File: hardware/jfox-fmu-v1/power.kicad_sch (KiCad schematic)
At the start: 7 parts, among them U20 LTC4417CGN, U21 TPS62132, U22 AP2112K-3.3, U23 AP22804AW5, U24 AP22804AW5, U25 AP22804AW5, U26 AP22804AW5

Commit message: Isolated CAN FD, and the short it took a bisect to find
CAN redundancy is resolved by using Cyphal. FDCAN1 and FDCAN2 become two
redundant Cyphal/CAN interfaces on two independent isolated buses.

That is not the compromise it looked like. Cyphal handles redundancy in the
protocol: the specification defines redundant transport groups where a node
publishes on every interface and the receiver deduplicates, per frame or per
transfer. libcanard gives each redundant interface its own TX queue for
exactly this. So two controllers is the arrangement Cyphal is built around,
and it buys controller-level redundancy rather than the isolator-level
redundancy that keeping two separate buses would have given. The "four
controllers needed, two available" constraint dissolves rather than binds.

Better still, if wanted later: Cyphal supports heterogeneous redundancy, so a
Cyphal/CAN interface paired with Cyphal/UDP would give dissimilar transport
redundancy - the same argument that puts three IMUs from two vendors here.

U30/U31 become ISOW1044: isolated CAN FD with an integrated isolated DC-DC, so
each bus gets its own supply domain without a separate converter. Two
datasheet shorts that are easy to miss and both mandatory (SLLSFF7A table
7-1): GNDIO and GND1 are not internally connected, and VISOOUT/VSIN/VISOIN are
one node. EN/FLT is wired as the fault output with a 10k pull-up, because a
redundant link whose failure is silent is not redundant.

And the bug. Swapping an 8-pin TCAN332 for a 20-pin ISOW1044 while leaving the
row pitch at 44.45 mm overlapped the two transceivers - the ISOW1044 spans
35.56 mm and 50.8 mm with its stubs. Their stub ends coincided and merged the
rails. The netlist came out with no GND net and no +5V net at all: 171 pins on
+3V3, ground shorted to the supply across the entire board.

Nothing caught it. ERC does not object to a short - it is well-formed. The
page-fit and footprint checks passed. Even "all MCU supply pins sit on their
rail" passed, beca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
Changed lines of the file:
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@@
 		(instances
 			(project "jfox-fmu"
-				(path "/fe62e68e-253a-4417-b7f1-ea7e59f14f88"
+				(path "/02ba8b64-ca25-47e9-8116-e586bde38a84"
 					(reference "U20")
 					(unit 1)
@@
 	(wire
 		(pts
-			(xy 64.77 134.62) (xy 64.77 142.24)
+			(xy 64.77 134.62) (xy 64.77 138.43)
 		)
 		(stroke
@@
 	(global_label "GND"
 		(shape input)
-		(at 64.77 142.24 180)
+		(at 64.77 138.43 180)
 		(fields_autoplaced yes)
 		(effects
@@
 		(instances
 			(project "jfox-fmu"
-				(path "/fe62e68e-253a-4417-b7f1-ea7e59f14f88"
+				(path "/02ba8b64-ca25-47e9-8116-e586bde38a84"
 					(reference "U21")
 					(unit 1)
@@
 	(wire
 		(pts
-			(xy 142.24 96.52) (xy 142.24 104.14)
+			(xy 142.24 96.52) (xy 142.24 100.33)
 		)
 		(stroke
@@
 	(global_label "GND"
 		(shape input)
-		(at 142.24 104.14 180)
+		(at 142.24 100.33 180)
 		(fields_autoplaced yes)
 		(effects
@@
 	(wire
 		(pts
-			(xy 142.24 71.12) (xy 142.24 63.5)
+			(xy 142.24 71.12) (xy 142.24 67.31)
 		)
 		(stroke
@@
 	(global_label "+5V"
 		(shape input)
-		(at 142.24 63.5 180)
+		(at 142.24 67.31 180)
 		(fields_autoplaced yes)
 		(effects
@@
 		(instances
 			(project "jfox-fmu"
-				(path "/fe62e68e-253a-4417-b7f1-ea7e59f14f88"
+				(path "/02ba8b64-ca25-47e9-8116-e586bde38a84"
 					(reference "U22")
 					(unit 1)
@@
 	(wire
 		(pts
-			(xy 142.24 147.32) (xy 142.24 154.94)
+			(xy 142.24 147.32) (xy 142.24 151.13)
 		)
 		(stroke
@@
 	(global_label "GND"
 		(shape input)
-		(at 142.24 154.94 180)
+		(at 142.24 151.13 180)
 		(fields_autoplaced yes)
 		(effects
@@
 		(instances
 			(project "jfox-fmu"
-				(path "/fe62e68e-253a-4417-b7f1-ea7e59f14f88"
+				(path "/02ba8b64-ca25-47e9-8116-e586bde38a84"
 					(reference "U23")
 					(unit 1)
@@
 	(wire
 		(pts
-			(xy 78.74 196.85) (xy 78.74 204.47)
+			(xy 78.74 196.85) (xy 78.74 200.66)
 		)
 		(stroke
@@
 	(global_label "GND"
 		(shape input)
-		(at 78.74 204.47 180)
+		(at 78.74 200.66 180)
 		(fields_autoplaced yes)
 		(effects
@@
 		(instances
 			(project "jfox-fmu"
-				(path "/fe62e68e-253a-4417-b7f1-ea7e59f14f88"
+				(path "/02ba8b64-ca25-47e9-8116-e586bde38a84"
 					(reference "U24")
 					(unit 1)
@@
 	(wire
 		(pts
-			(xy 157.48 196.85) (xy 157.48 204.47)
+			(xy 157.48 196.85) (xy 157.48 200.66)
 		)
 		(stroke
@@
 	(global_label "GND"
 		(shape input)
-		(at 157.48 204.47 180)
+		(at 157.48 200.66 180)
 		(fields_autoplaced yes)
 		(effects
@@
 		(instances
 			(project "jfox-fmu"
-				(path "/fe62e68e-253a-4417-b7f1-ea7e59f14f88"
+				(path "/02ba8b64-ca25-47e9-8116-e586bde38a84"
 					(reference "U25")
 					(unit 1)
@@
 	(wire
 		(pts
-			(xy 78.74 241.3) (xy 78.74 248.92)
+			(xy 78.74 241.3) (xy 78.74 245.11)
 		)
 		(stroke
@@
 	(global_label "GND"
 		(shape input)
-		(at 78.74 248.92 180)
+		(at 78.74 245.11 180)
 		(fields_autoplaced yes)
 		(effects
@@
 		(instances
 			(project "jfox-fmu"
-				(path "/fe62e68e-253a-4417-b7f1-ea7e59f14f88"
+				(path "/02ba8b64-ca25-47e9-8116-e586bde38a84"
 					(reference "U26")
 					(unit 1)
@@
 	(wire
 		(pts
-			(xy 157.48 241.3) (xy 157.48 248.92)
+			(xy 157.48 241.3) (xy 157.48 245.11)
 		)
 		(stroke
@@
 	(global_label "GND"
 		(shape input)
-		(at 157.48 248.92 180)
-		(fields_autoplaced yes)
-		(effects
+		(at 157.48 245.11 180)
+		(fields_autoplaced yes)
+		(effects

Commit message: Five connections that went nowhere, and the pin name that hid one
None of these were visible as failures. Every one was a wire drawn to a name
that did not exist, which KiCad accepts silently.

wire_part matches by pin NAME. Four keys in the comms sheet matched nothing:

  "DAT3/CS"  the microSD symbol's pin is "CD/DAT3", so SDMMC1_D3 reached the
             MCU and stopped. The card would have run in 1-bit mode at best.
  "DET"      this symbol has no card-detect pin at all, so SD_DETECT had no
             source. Recorded rather than faked - it needs a socket symbol
             that exposes CD.
  "VSS2"     does not exist on this symbol.
  "SBU1/2"   do not exist on the USB-C symbol.

PC2 is the one worth remembering. On this package PC2 and PC3 exist only as
PC2_C and PC3_C - the analog-switch-capable balls. plan_pinout works from the
chip's alternate-function table, which calls them PC2 and PC3, so the lookup
missed and the allocated signal went nowhere. Aliased in both the generator
and the checker, which is what surfaced it: the check reported "symbol has no
pin named PC2" the moment the allocation grew enough to reach that pin.

Four parts that were missing outright, each leaving a function non-functional:

  R9/R10   5.1k on USB CC1/CC2. Without them the port is not a USB-C sink and
           no host will enumerate it. The CC pins reached the connector and
           nothing else.
  R11/R12  VBUS sense divider. VBUS_SENSE reached an ADC pin with nothing
           driving it. 10k/10k puts 5.25 V at 2.63 V, inside the reference.
  R13-R16  pull-ups on the four load-switch fault outputs, which are open
           drain and were unreadable without them.

And ten status signals now reach the MCU that previously reached nothing:
BRICK_VALID, SERVO_VALID, USB_VALID, PG_3V3, the four rail fault flags and
both isolator fault outputs. The board could not previously tell whether its
power source was valid, whether a sensor rail had tripped, or whether an
isolated 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
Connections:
- net +3V3_IMU1_FLG renamed IMU1_RAIL_FLG
- net +3V3_IMU2_FLG renamed IMU2_RAIL_FLG
- net +3V3_IMU3_FLG renamed IMU3_RAIL_FLG
- net +3V3_SENS_FLG renamed SENS_RAIL_FLG
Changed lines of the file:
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@@
 		(instances
 			(project "jfox-fmu"
-				(path "/02ba8b64-ca25-47e9-8116-e586bde38a84"
+				(path "/4872ddcb-93c6-49fe-aa11-f13239158285"
 					(reference "U20")
 					(unit 1)
@@
 		(instances
 			(project "jfox-fmu"
-				(path "/02ba8b64-ca25-47e9-8116-e586bde38a84"
+				(path "/4872ddcb-93c6-49fe-aa11-f13239158285"
 					(reference "U21")
 					(unit 1)
@@
 		(instances
 			(project "jfox-fmu"
-				(path "/02ba8b64-ca25-47e9-8116-e586bde38a84"
+				(path "/4872ddcb-93c6-49fe-aa11-f13239158285"
 					(reference "U22")
 					(unit 1)
@@
 		(instances
 			(project "jfox-fmu"
-				(path "/02ba8b64-ca25-47e9-8116-e586bde38a84"
+				(path "/4872ddcb-93c6-49fe-aa11-f13239158285"
 					(reference "U23")
 					(unit 1)
@@
 		)
 	)
-	(global_label "+3V3_IMU1_FLG"
-		(shape input)
+	(global_label "IMU1_RAIL_FLG"
+		(shape bidirectional)
 		(at 96.52 191.77 180)
 		(fields_autoplaced yes)
@@
 		(instances
 			(project "jfox-fmu"
-				(path "/02ba8b64-ca25-47e9-8116-e586bde38a84"
+				(path "/4872ddcb-93c6-49fe-aa11-f13239158285"
 					(reference "U24")
 					(unit 1)
@@
 		)
 	)
-	(global_label "+3V3_IMU2_FLG"
-		(shape input)
+	(global_label "IMU2_RAIL_FLG"
+		(shape bidirectional)
 		(at 175.26 191.77 180)
 		(fields_autoplaced yes)
@@
 		(instances
 			(project "jfox-fmu"
-				(path "/02ba8b64-ca25-47e9-8116-e586bde38a84"
+				(path "/4872ddcb-93c6-49fe-aa11-f13239158285"
 					(reference "U25")
 					(unit 1)
@@
 		)
 	)
-	(global_label "+3V3_IMU3_FLG"
-		(shape input)
+	(global_label "IMU3_RAIL_FLG"
+		(shape bidirectional)
 		(at 96.52 236.22 180)
 		(fields_autoplaced yes)
@@
 		(instances
 			(project "jfox-fmu"
-				(path "/02ba8b64-ca25-47e9-8116-e586bde38a84"
+				(path "/4872ddcb-93c6-49fe-aa11-f13239158285"
 					(reference "U26")
 					(unit 1)
@@
 		)
 	)
-	(global_label "+3V3_SENS_FLG"
-		(shape input)
+	(global_label "SENS_RAIL_FLG"
+		(shape bidirectional)
 		(at 175.26 236.22 180)
 		(fields_autoplaced yes)

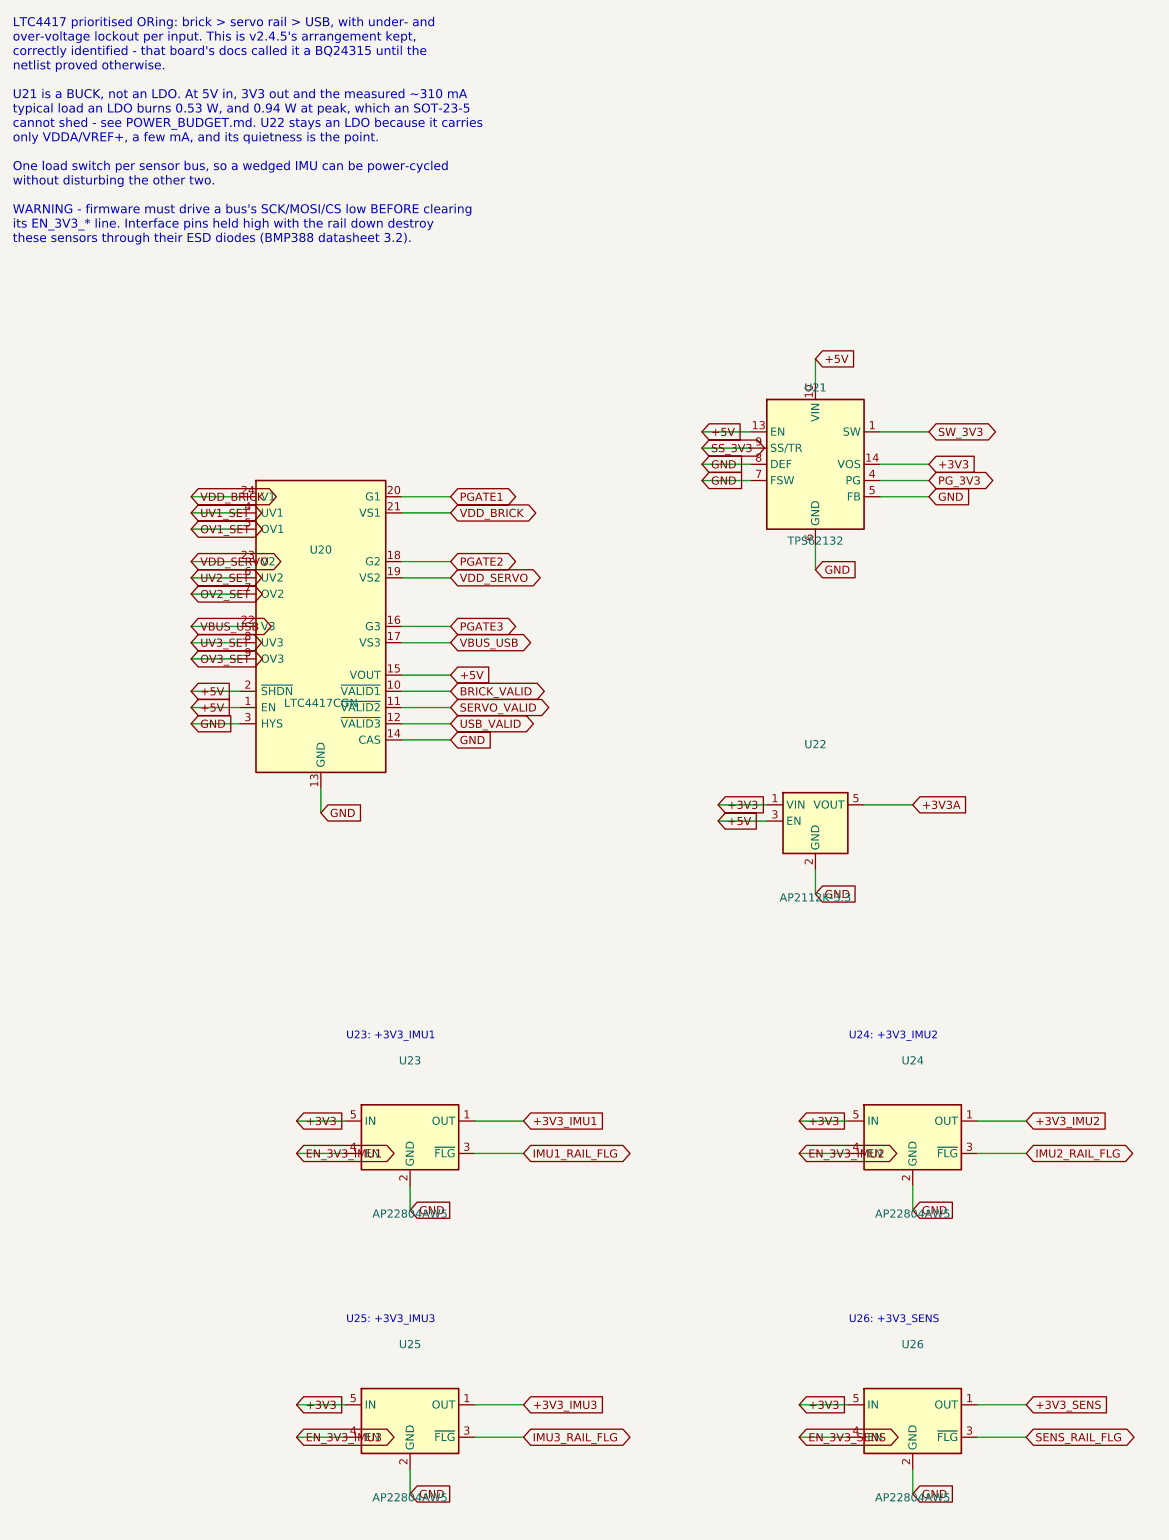
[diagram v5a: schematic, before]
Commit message: The ORing controller had no switches and no thresholds
With the LTC4417 datasheet in hand, the last of the connections close.
Isolated nets 10 -> 1.

PGATE1-3 drove nothing and UV/OV_SET went nowhere, so U20 sat on the board
arbitrating between three inputs it could neither measure nor switch. Both
halves are now built:

Two back-to-back PMOS per input, sources common, gates both on Gn. That is
what "blocks reverse AND cross conduction" on the datasheet's front page
actually requires - one FET's body diode faces each way. A single FET per
channel leaves a permanent diode path and the ORing does nothing.

And VS1-3 were wired straight to the input rails. VSn senses the FET common
source (ADI figure 1), so the design was measuring the wrong side of a switch
that did not exist.

Thresholds from ADI's equations, with UV taking the middle tap and OV the
bottom one:

    UV = Rtot / (Rmid + Rbot)        OV = Rtot / Rbot

Checked by reproducing the datasheet's own worked example before using them:
806k/39.2k/60.4k gives 9.09 V and 14.99 V, which is what figure 1 labels for a
12 V adapter. Then applied per input - brick 4.52/5.81 V, servo 4.54/6.55 V
because BECs are commonly 5 V or 6 V, USB 4.38/5.47 V.

Two BOM errors the datasheet also settled:

The LTC4417 is a 24-lead part. It carried Package_SO:SSOP-16 - a real
footprint, a real name, eight pads short, and unbuildable. check_fmu_footprints
was verifying that a name RESOLVES, never that it matches the part, so this
passed every run. It now compares pad count against pin count.

That check concealed itself twice while being written, in the way this file
has form for: `mismatched` was not added to the total, so the count silently
dropped by one and printed PASS; then `good` did not include it either, so it
printed FAIL and exited 0. Both fixed, and the total now carries a comment
saying why every failure category must be in it.

And the datasheet's ordering table lists only I (-40/+85) and H (-40/+125)
grades - there is 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
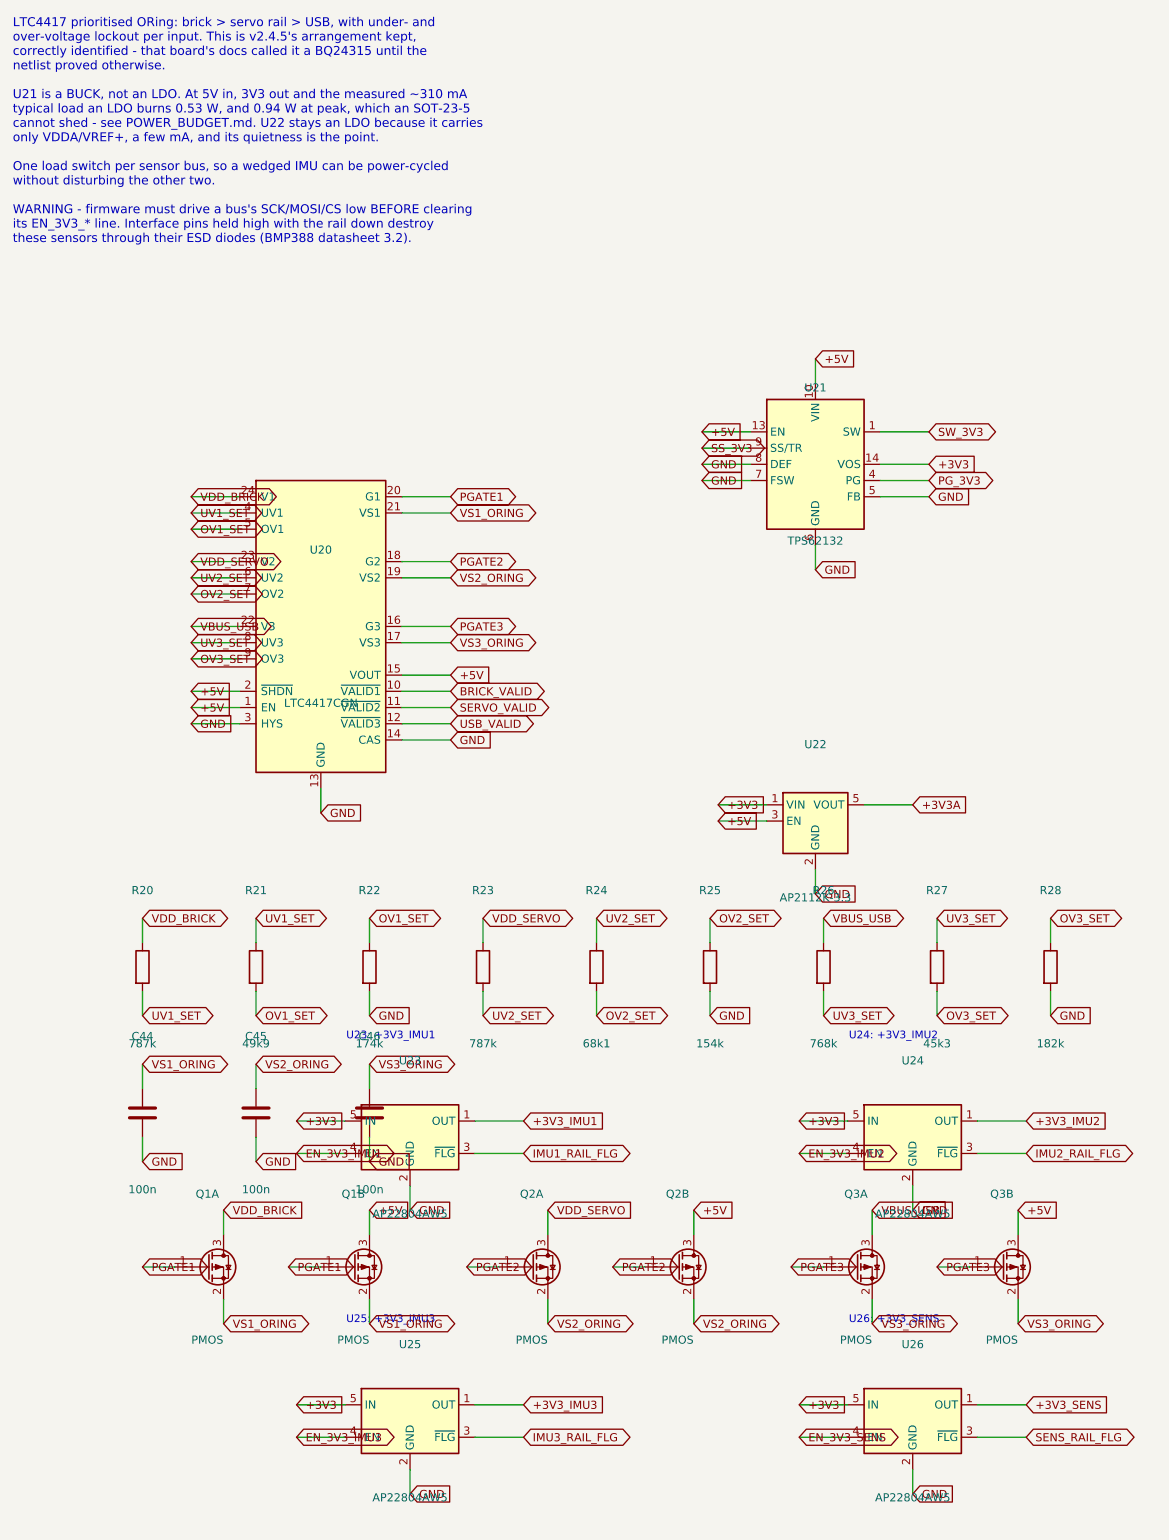
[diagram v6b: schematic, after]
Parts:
- added C44, C45, C46: 100n, Capacitor_SMD:C_0402_1005Metric, symbol Device:C
- added Q1A, Q1B, Q2A, Q2B, Q3A, Q3B: PMOS, Package_TO_SOT_SMD:SOT-23, symbol Transistor_FET:Q_PMOS_GSD
- added R20, R23: 787k, Resistor_SMD:R_0402_1005Metric, symbol Device:R
- added R21: 49k9, Resistor_SMD:R_0402_1005Metric, symbol Device:R
- added R22: 174k, Resistor_SMD:R_0402_1005Metric, symbol Device:R
- added R24: 68k1, Resistor_SMD:R_0402_1005Metric, symbol Device:R
- added R25: 154k, Resistor_SMD:R_0402_1005Metric, symbol Device:R
- added R26: 768k, Resistor_SMD:R_0402_1005Metric, symbol Device:R
- added R27: 45k3, Resistor_SMD:R_0402_1005Metric, symbol Device:R
- added R28: 182k, Resistor_SMD:R_0402_1005Metric, symbol Device:R
- U20: footprint Package_SO:SSOP-16_3.9x4.9mm_P0.635mm -> Package_SO:SSOP-24_3.9x8.7mm_P0.635mm
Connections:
- net +5V: now also Q1B.3 (D), Q2B.3 (D), Q3B.3 (D)
- net GND: now also C44.2, C45.2, C46.2, R22.2, R25.2, R28.2
- net OV1_SET: now also R21.2, R22.1
- net OV2_SET: now also R24.2, R25.1
- net OV3_SET: now also R27.2, R28.1
- net PGATE1: now also Q1A.1 (G), Q1B.1 (G)
- net PGATE2: now also Q2A.1 (G), Q2B.1 (G)
- net PGATE3: now also Q3A.1 (G), Q3B.1 (G)
- net UV1_SET: now also R20.2, R21.1
- net UV2_SET: now also R23.2, R24.1
- net UV3_SET: now also R26.2, R27.1
- net VBUS_USB: now also Q3A.3 (D), R26.1; no longer U20.17 (VS3)
- net VDD_BRICK: now also Q1A.3 (D), R20.1; no longer U20.21 (VS1)
- net VDD_SERVO: now also Q2A.3 (D), R23.1; no longer U20.19 (VS2)
- new net VS1_ORING: C44.1, Q1A.2 (S), Q1B.2 (S), U20.21 (VS1)
- new net VS2_ORING: C45.1, Q2A.2 (S), Q2B.2 (S), U20.19 (VS2)
- new net VS3_ORING: C46.1, Q3A.2 (S), Q3B.2 (S), U20.17 (VS3)
